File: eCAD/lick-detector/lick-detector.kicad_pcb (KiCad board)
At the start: 4 copper layers, 25 x 45 mm, 72 parts, among them J1 J_PinHeader_01x03_2.54_V, J2 J_PinHeader_01x02_2.54_V, J3 J_PinHeader_01x02_2.54_V, J4 J_PinHeader_01x02_2.54_V, J5 J_PinHeader_01x02_2.54_V, J6 J_PinHeader_01x02_2.54_V, J7 J_PinHeader_01x02_2.54_V, J8 J_PinHeader_01x02_2.54_V, J9 J_PinHeader_01x02_2.54_V, U1 LM27762DSSR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

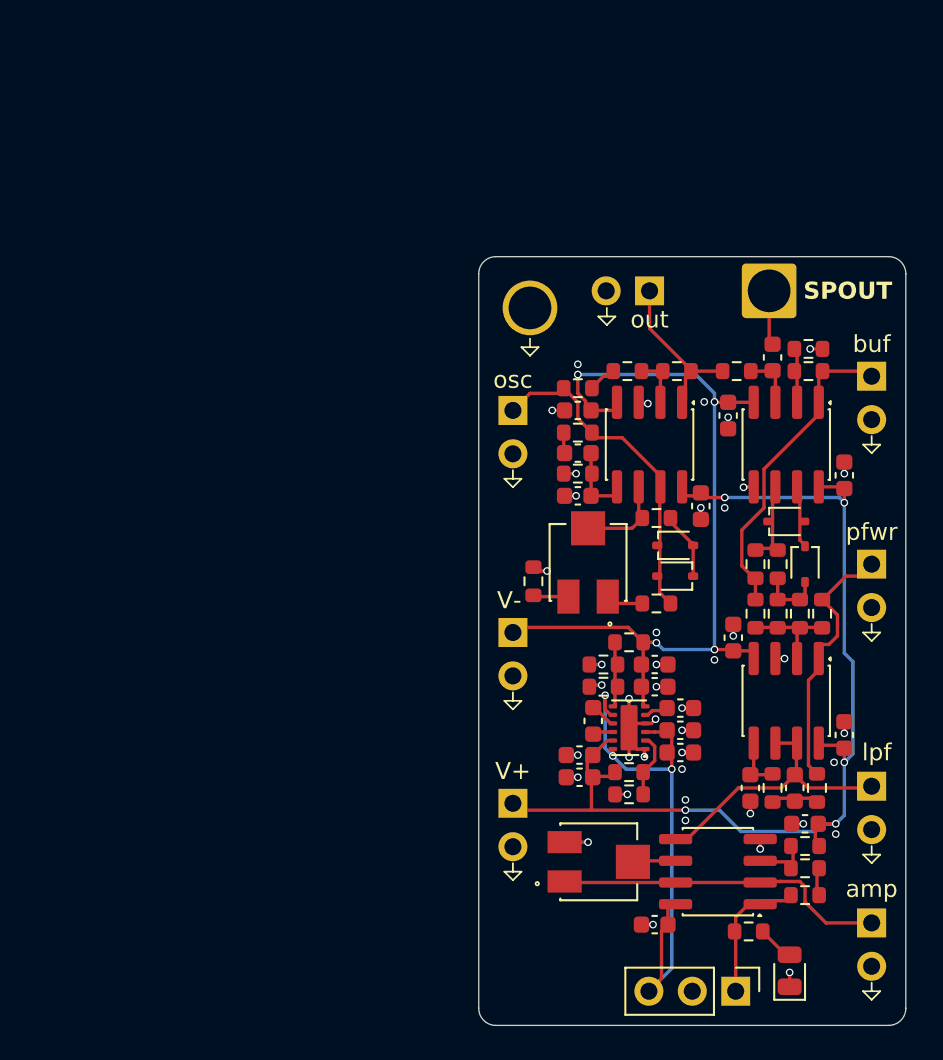
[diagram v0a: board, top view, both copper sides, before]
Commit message: Number of upgrades complete: - Lower amplitude sine wave generator - Improved debug connector layout - Brightness of LED decreased - README updated with guide and areas for documentation - .gitignore added to ignore backup files and temporary files
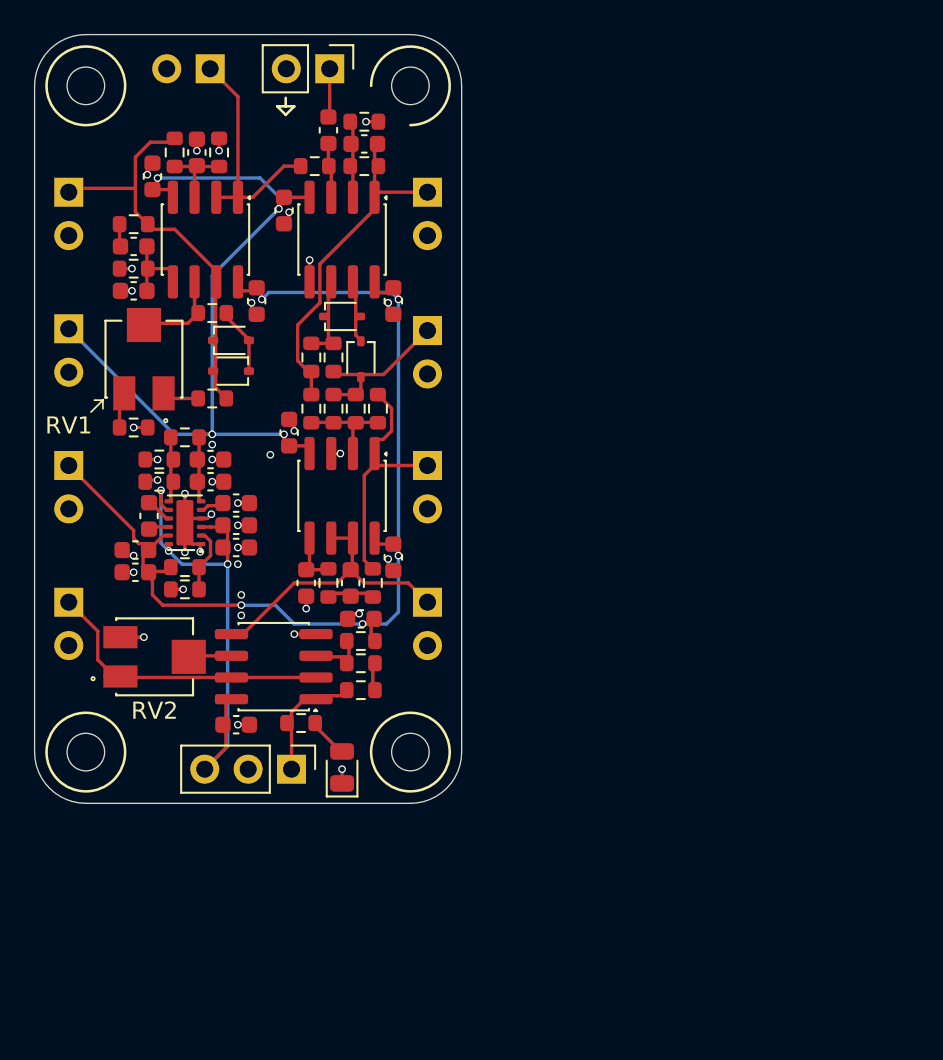
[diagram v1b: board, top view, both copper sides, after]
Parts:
- removed ? (x2): , 
- removed C12: 10n, !fablabs-kicad-library:C_0603_1608M
- removed R19, R27, R28: 1k, !fablabs-kicad-library:R_0603_1608M
- added C23: 100p, !fablabs-kicad-library:C_0603_1608M, F.Cu at (159.3, 81.4)
- added C24: 100p, !fablabs-kicad-library:C_0603_1608M, F.Cu at (149.5, 81.9)
- added C25: 1n, !fablabs-kicad-library:C_0603_1608M, F.Cu at (157.2, 80.6)
- added J10: J_PinHeader_01x02_2.54_V, !fablabs-kicad-library:J_PinHeader_01x02_2.54_V, B.Cu at (163.0, 92.3)
- added J11: J_PinHeader_01x02_2.54_V, !fablabs-kicad-library:J_PinHeader_01x02_2.54_V, F.Cu at (157.3, 77.0)
- added R30: 1k, !fablabs-kicad-library:R_0603_1608M, F.Cu at (156.2, 93.9)
- added R31: 1k, !fablabs-kicad-library:R_0603_1608M, F.Cu at (157.5, 93.9)
- R12: value 10k -> 100k
- R22: value 220R -> 10k
- R6: value 10k -> 470R
- moved J9 50.6 mm to (142.0, 108.2)
- moved R12 42.7 mm to (148.2, 81.9), turned to 90 degrees
- moved R10 39.6 mm to (150.8, 81.9), turned to -90 degrees
- moved J2 32.7 mm to (142.0, 100.2)
- moved J3 31.5 mm to (142.0, 92.2)
- moved J1 29.1 mm to (155.0, 118.0)
- moved J7 29.0 mm to (142.0, 84.2)
- moved R22 28.9 mm to (155.6, 115.3)
- moved J8 28.8 mm to (150.3, 77.0)
- moved D5 28.8 mm to (158.0, 117.9)
- moved R25 28.7 mm to (145.8, 86.1)
- moved C19 28.7 mm to (145.8, 87.4)
- moved C1 28.6 mm to (151.8, 102.4)
- moved C10 28.6 mm to (154.6, 85.3)
- moved C11 28.6 mm to (145.9, 106.5)
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- renumbered RV2 to RV1, RV3 to RV2
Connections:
- D1 pad 2: Net-(D1-A) -> /RMS-to-DC/hwr
- R10 pad 1: /RMS-to-DC/buf -> GND
- R10 pad 2: Net-(D3-K) -> Net-(U3A-+)
- R12 pad 1: Net-(D3-K) -> Net-(U3A-+)
- R12 pad 2: Net-(D1-A) -> /sine-wave-generator/osc
- R13 pad 1: Net-(D1-A) -> /RMS-to-DC/hwr
- R14 pad 1: Net-(D1-A) -> /RMS-to-DC/hwr
- R6 pad 1: Net-(R27-Pad1) -> GND
- R6 pad 2: Net-(U3A--) -> Net-(U4A--)
- U3 pad 2: Net-(U3A--) -> /sine-wave-generator/out
- U3 pad 3: GND -> Net-(U3A-+)
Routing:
- net /RMS-to-DC/hwr: track 0.00 -> 9.64 mm
- net Net-(U3A-+): track 0.00 -> 4.51 mm
- net /sine-wave-generator/out: track 9.49 -> 13.9 mm
- net /sine-wave-generator/osc: track 19.6 -> 23.8 mm
- net Net-(D1-A): track 4.12 -> 0.00 mm
- net GND: track 28.4 -> 31.5 mm, vias 43 -> 39
- net V+: track 63.5 -> 66.4 mm
- net Net-(U3A--): track 2.73 -> 0.00 mm
- net /RMS-to-DC/buf: track 18.8 -> 21.2 mm
- net V-: track 49.4 -> 51.6 mm
- net Net-(R27-Pad1): track 1.78 -> 0.00 mm
- net VCC: track 33.0 -> 31.5 mm
- net /schmitt-trigger/amp: track 19.7 -> 18.2 mm
- net Net-(U4A--): track 3.19 -> 4.49 mm
- net /schmitt-trigger/out: track 8.47 -> 7.47 mm
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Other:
- outline, holes or cut-outs redrawn
- board text added: "-GND"
- board text added: "-TTL"
- board text added: "-VCC"
- board text added: "= GND"
- board text added: "Lick Detector Capacitive V1.0"
- board text added: "RV1"
- board text added: "RV2"
- board text added: "hwr"
- board text removed: "156kHz 400mV p-p"
- board text removed: "Lick Detector"
